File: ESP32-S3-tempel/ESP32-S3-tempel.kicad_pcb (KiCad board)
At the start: 2 copper layers, 33 parts, among them J1 USB_C_Receptacle_USB2.0_14P, J2 USB_C_Receptacle_USB2.0_14P, J3 West, J4 East, J5 Nort, J6 South, Q1 SS8050, Q2 SS8050, SW1 RST, SW2 Boot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

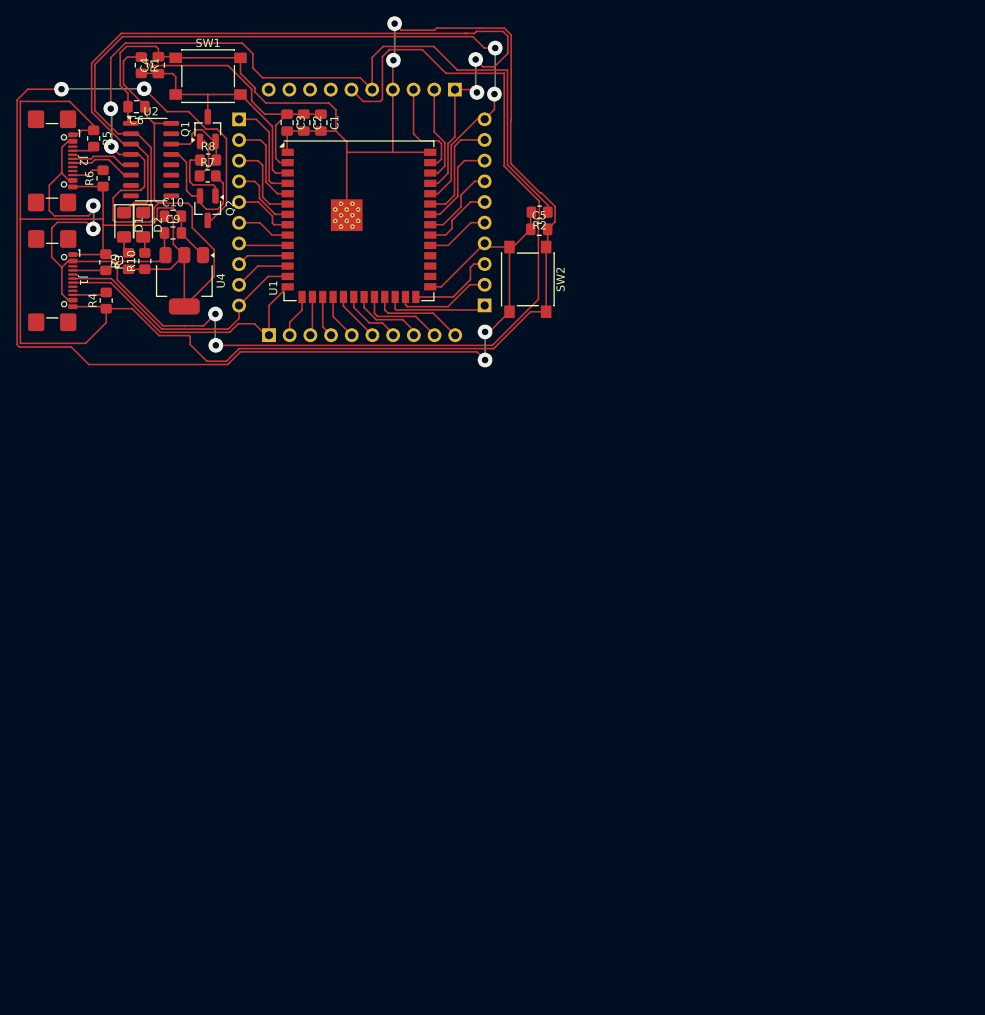
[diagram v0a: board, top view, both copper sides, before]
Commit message: feat: finish routing and tidyng silkscreen
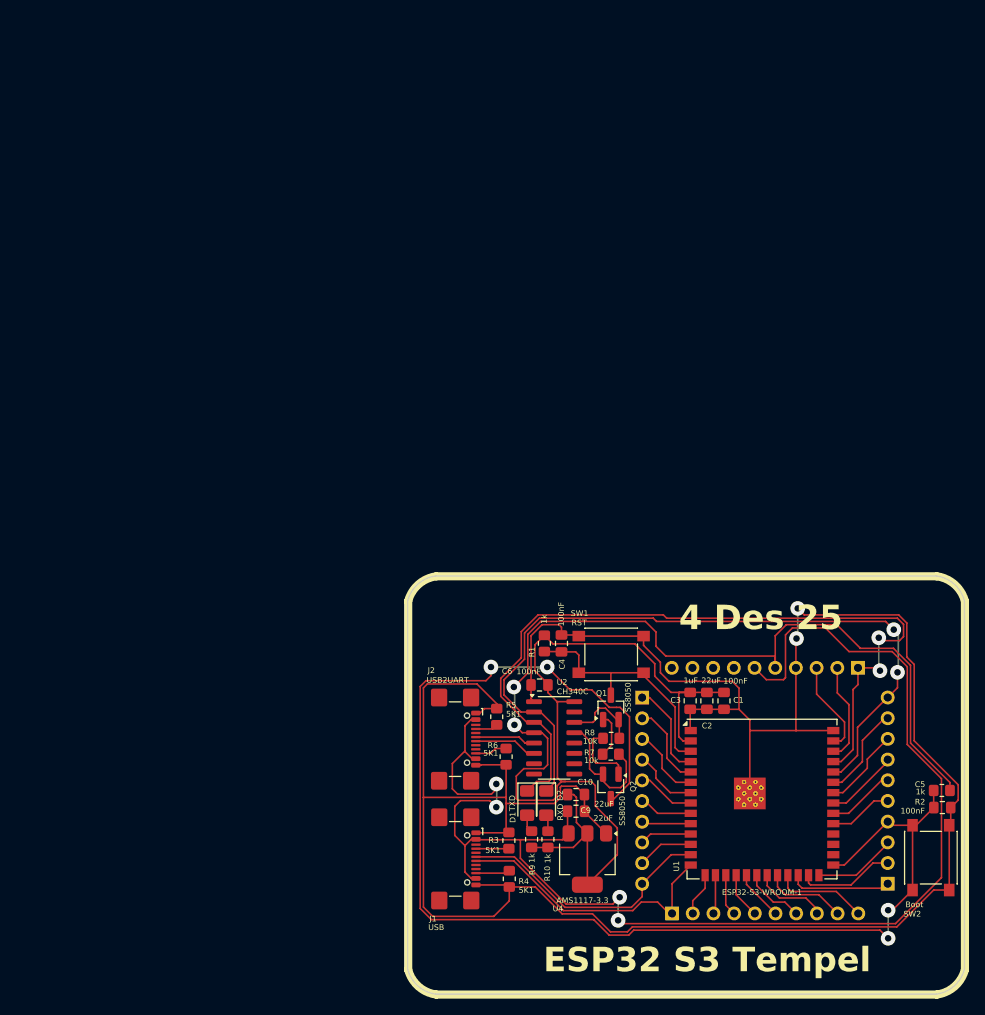
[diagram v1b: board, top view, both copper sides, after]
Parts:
- J1: value USB_C_Receptacle_USB2.0_14P -> USB
- J2: value USB_C_Receptacle_USB2.0_14P -> USB2UART
- moved C10 86.5 mm to (144.7, 107.9)
- moved C4 86.5 mm to (142.9, 89.4)
- moved C5 86.5 mm to (189.7, 109.5)
- moved C6 86.5 mm to (140.2, 94.5)
- moved D1 86.5 mm to (138.7, 109.0)
- moved D2 86.5 mm to (141.1, 109.0)
- moved J1 86.5 mm to (128.8, 115.8)
- moved J2 86.5 mm to (128.7, 101.1)
- moved J3 86.5 mm to (152.8, 96.0)
- moved J4 86.5 mm to (183.0, 118.9)
- moved J5 86.5 mm to (179.3, 92.4)
- moved J6 86.5 mm to (156.5, 122.5)
- moved Q1 86.5 mm to (149.0, 97.2)
- moved R1 86.5 mm to (140.8, 89.4)
- moved R10 86.5 mm to (141.3, 113.4)
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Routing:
- net GND: track 306.4 -> 298.1 mm
- net /TXD0: track 104.8 -> 99.6 mm
- net /RXD0: track 96.3 -> 93.0 mm
- net +3.3V: track 208.5 -> 206.2 mm
- net +5V: track 172.3 -> 170.3 mm
- net /IO42: track 13.4 -> 11.5 mm
- net /IO0: track 163.4 -> 161.6 mm
- net /IO41: track 11.5 -> 10.1 mm
- net /IO6: track 10.5 -> 9.14 mm
- net /IO1: track 12.8 -> 11.5 mm
- net /IO4: track 12.7 -> 11.7 mm
- net /IO5: track 11.3 -> 10.5 mm
- net /IO45: track 11.0 -> 10.2 mm
- net /IO40: track 9.74 -> 9.03 mm
- net /IO39: track 8.94 -> 8.36 mm
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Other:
- board outline added: 68.4 x 51.3 mm
- board text added: "4 Des 25"
- board text added: "ESP32 S3 Tempel"
